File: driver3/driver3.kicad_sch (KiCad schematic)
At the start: 23 parts, among them J1 Conn_02x08_Odd_Even, J2 Conn_02x08_Counter_Clockwise, J3 Conn_01x05, J4 Conn_01x03_Pin, SW1 SW_DIP_x02, SW2 SW_DIP_x02, U1 MP6605CGR-Z

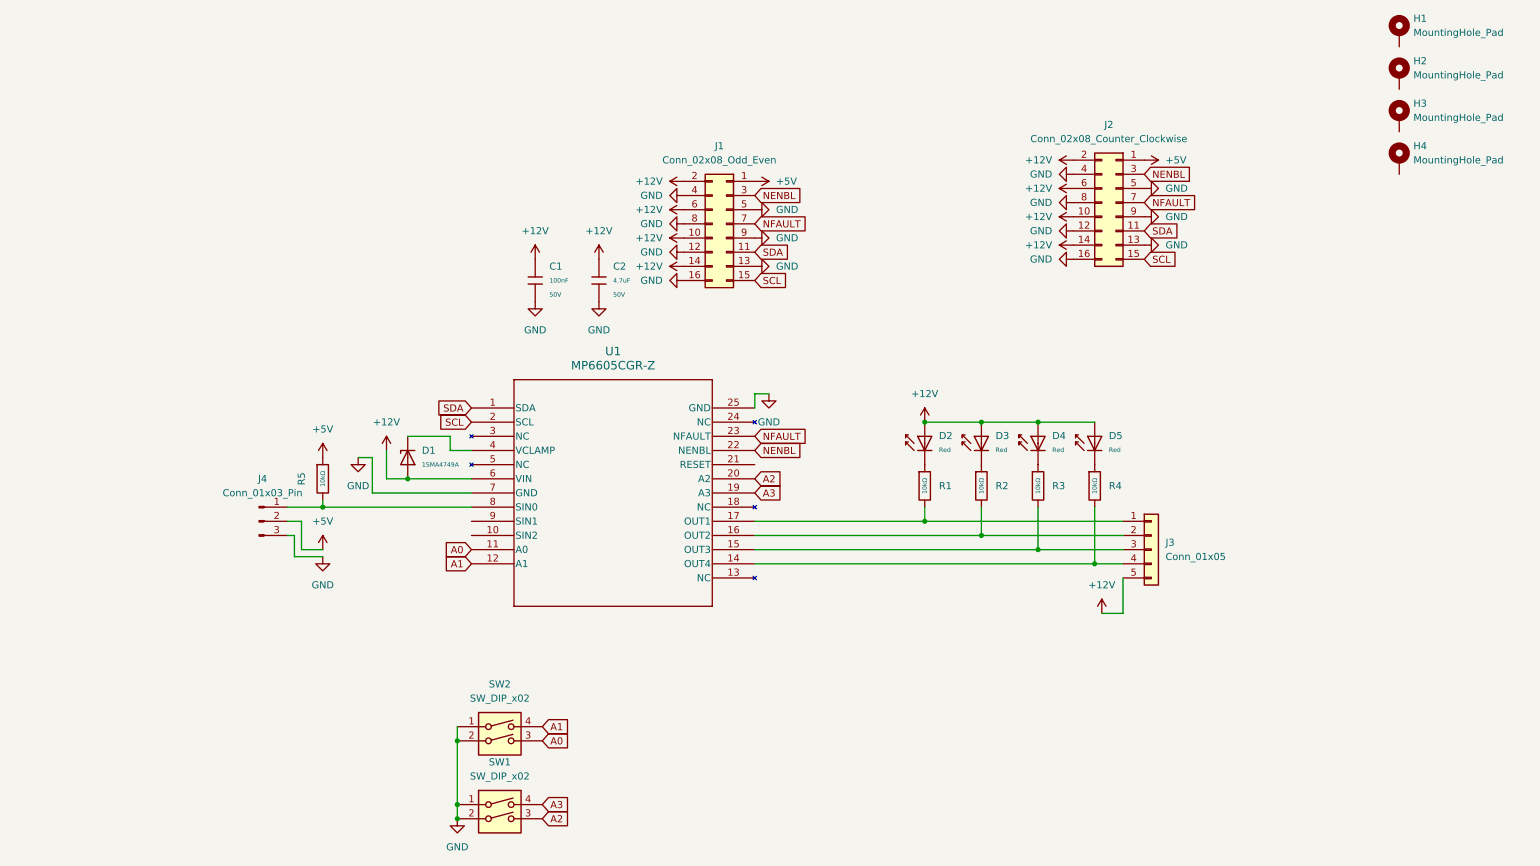
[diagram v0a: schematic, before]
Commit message: Add new driver and web client
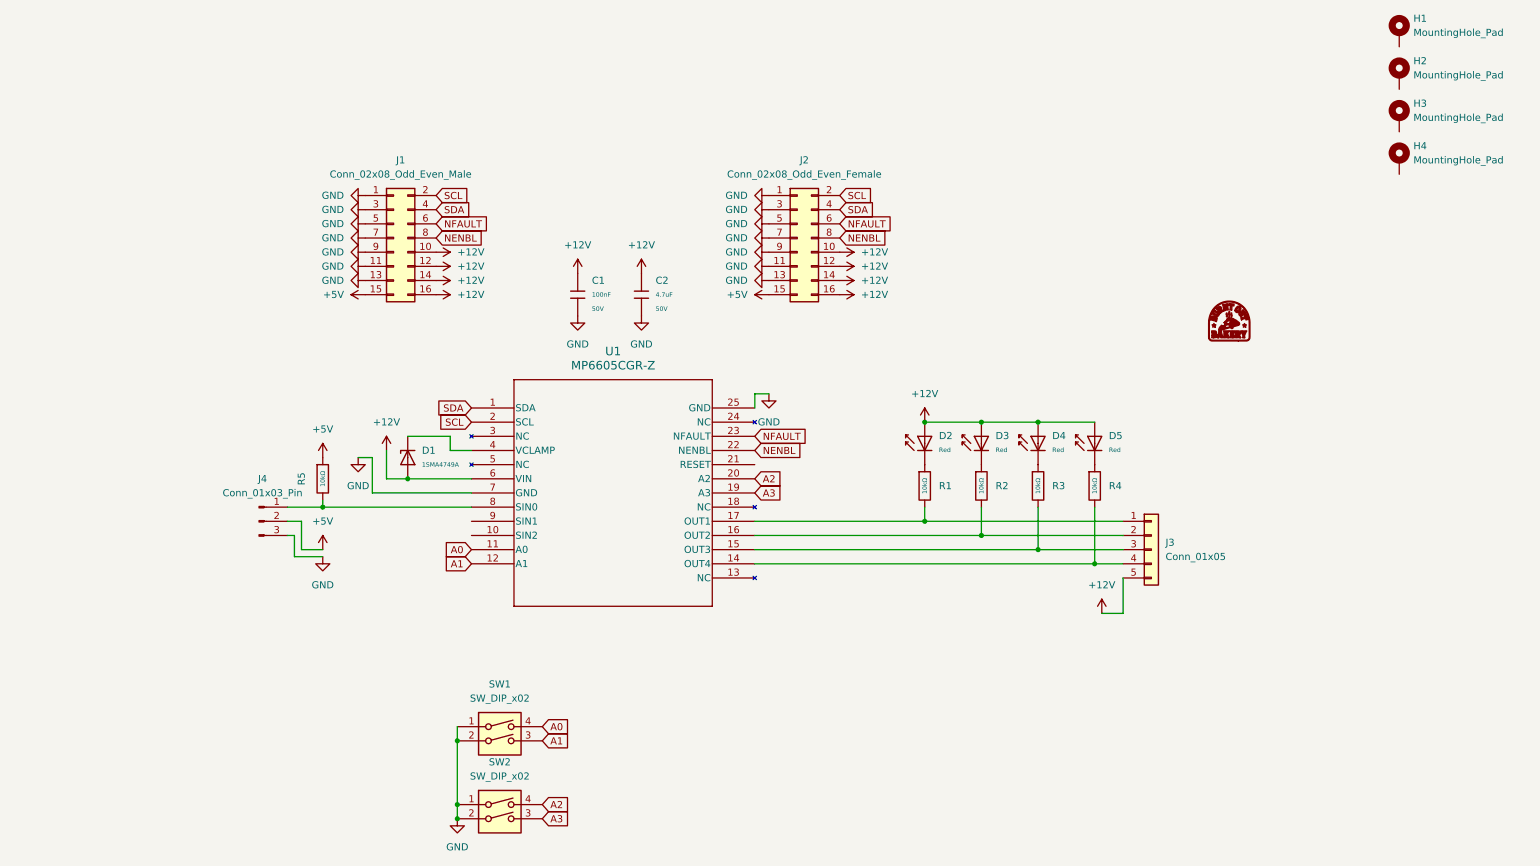
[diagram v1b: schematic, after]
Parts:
- added G1: LOGO, BurntOutBakery:BurntOutBakery, symbol BurntOutBakery:LOGO
- J1: value Conn_02x08_Odd_Even -> Conn_02x08_Odd_Even_Male
- J2: value Conn_02x08_Counter_Clockwise -> Conn_02x08_Odd_Even_Female
- renumbered SW2 to SW1, SW1 to SW2
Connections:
- net +12V: now also J1.12 (Pin_12), J1.16 (Pin_16), J2.12 (Pin_12), J2.16 (Pin_16); no longer J1.2 (Pin_2), J1.6 (Pin_6), J2.2 (Pin_2), J2.6 (Pin_6)
- net +5V: now also J1.15 (Pin_15), J2.15 (Pin_15); no longer J1.1 (Pin_1), J2.1 (Pin_1)
- net A0: now also SW1.4; no longer SW1.3
- net A1: now also SW1.3; no longer SW1.4
- net A2: now also SW2.4; no longer SW2.3
- net A3: now also SW2.3; no longer SW2.4
- net GND: now also J1.1 (Pin_1), J1.11 (Pin_11), J1.3 (Pin_3), J1.7 (Pin_7), J2.1 (Pin_1), J2.11 (Pin_11), J2.3 (Pin_3), J2.7 (Pin_7); no longer J1.12 (Pin_12), J1.16 (Pin_16), J1.4 (Pin_4), J1.8 (Pin_8), J2.12 (Pin_12), J2.16 (Pin_16), J2.4 (Pin_4), J2.8 (Pin_8)
- net NENBL: now also J1.8 (Pin_8), J2.8 (Pin_8); no longer J1.3 (Pin_3), J2.3 (Pin_3)
- net NFAULT: now also J1.6 (Pin_6), J2.6 (Pin_6); no longer J1.7 (Pin_7), J2.7 (Pin_7)
- net SCL: now also J1.2 (Pin_2), J2.2 (Pin_2); no longer J1.15 (Pin_15), J2.15 (Pin_15)
- net SDA: now also J1.4 (Pin_4), J2.4 (Pin_4); no longer J1.11 (Pin_11), J2.11 (Pin_11)
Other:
- moved on the sheet: C1, C2, J1, J2

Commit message: Go back to DRV8804 based design because the MP6605CGR seems to be out of stock.
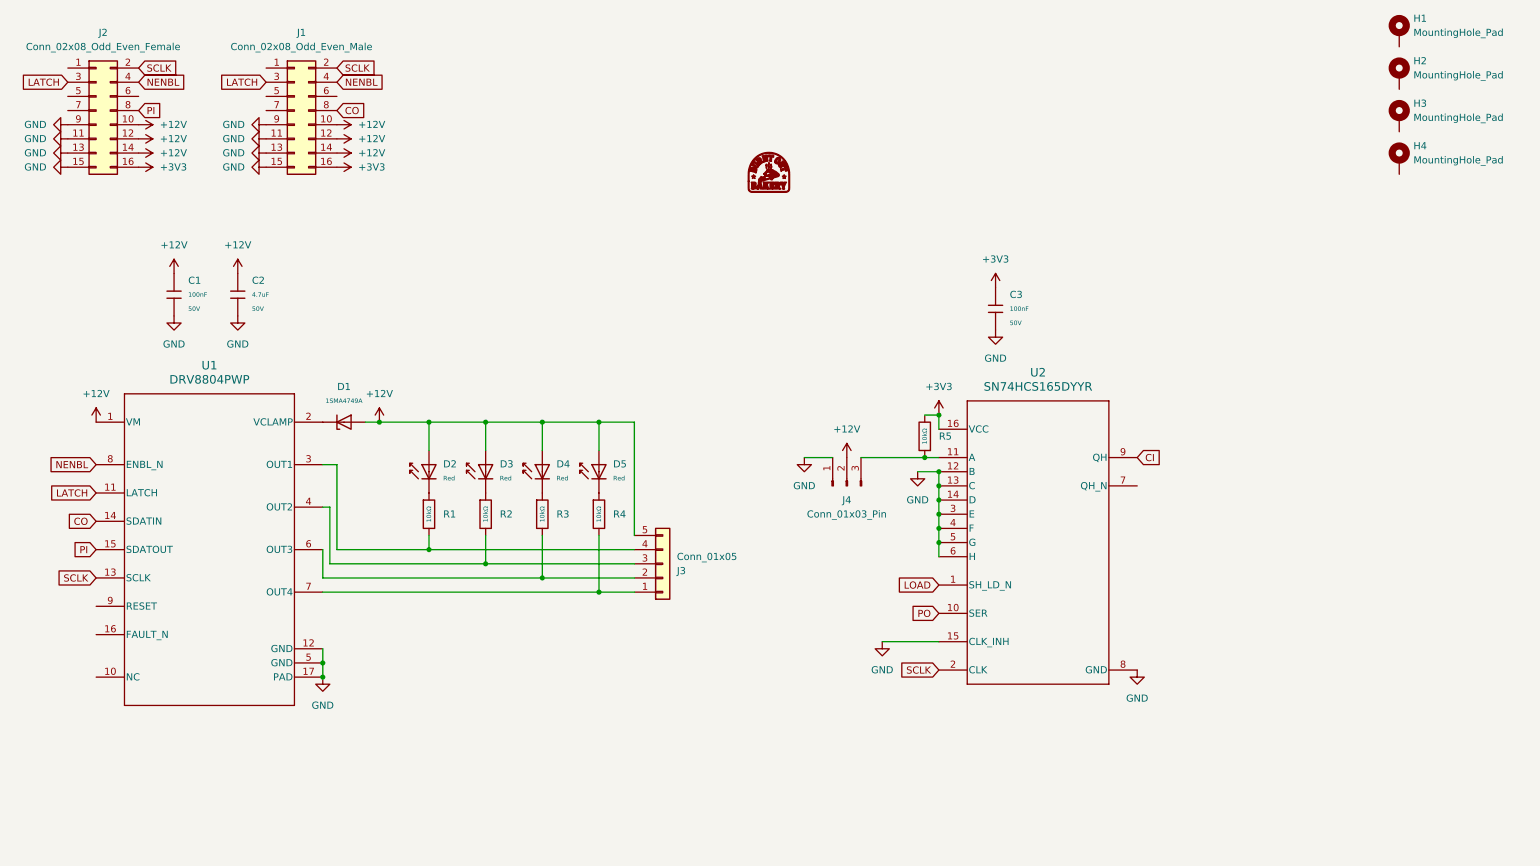
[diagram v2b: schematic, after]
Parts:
- removed SW1, SW2: SW_DIP_x02, Button_Switch_THT:SW_DIP_SPSTx02_Slide_9.78x7.26mm_W7.62mm_P2.54mm, symbol Switch:SW_DIP_x02
- removed U1: MP6605CGR-Z, QFN-24_MP6605C_MNP, symbol ul_MP6605CGR-Z:MP6605CGR-Z
- added C3: 100nF, PCM_JLCPCB:C_0603, symbol PCM_JLCPCB-Capacitors:0603,100nF
- added U1: DRV8804PWP, Package_SO:HTSSOP-16-1EP_4.4x5mm_P0.65mm_EP3.4x5mm_Mask3x3mm_ThermalVias, symbol ul_DRV8804PWP:DRV8804PWP
- added U2: SN74HCS165DYYR, DYY0016A-MFG, symbol ul_SN74HCS165DYYR:SN74HCS165DYYR
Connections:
- net SDA is gone; now on net NENBL: J1.4 (Pin_4), J2.4 (Pin_4)
- net +12V: now also J4.2 (Pin_2), U1.1 (VM); no longer J1.16 (Pin_16), J2.16 (Pin_16)
- net GND: now also J1.15 (Pin_15), J2.15 (Pin_15), J4.1 (Pin_1), C3.2, U1.12 (GND), U1.17 (PAD), U1.5 (GND), U2.12 (B), U2.13 (C), U2.14 (D), U2.15 (CLK_INH), U2.3 (E), U2.4 (F), U2.5 (G), U2.6 (H), U2.8 (GND); no longer J1.1 (Pin_1), J1.3 (Pin_3), J1.5 (Pin_5), J1.7 (Pin_7), J2.1 (Pin_1), J2.3 (Pin_3), J2.5 (Pin_5), J2.7 (Pin_7), J4.3 (Pin_3)
- net NENBL: now also U1.8 (ENBL_N); no longer J1.8 (Pin_8), J2.8 (Pin_8)
- net at R4.2: now also J3.1 (Pin_1), U1.7 (OUT4); no longer J3.4 (Pin_4)
- net at J3.3 (Pin_3): now also R2.2, U1.4 (OUT2); no longer R3.2
- net at J3.2 (Pin_2): now also R3.2, U1.6 (OUT3); no longer R2.2
- net at R1.2: now also J3.4 (Pin_4), U1.3 (OUT1); no longer J3.1 (Pin_1)
- net at D1.1: now also U1.2 (VCLAMP)
- net +3V3: now reaches R5.2
- net +3V3: now also J1.16 (Pin_16), J2.16 (Pin_16), C3.1, U2.16 (VCC); no longer J4.1 (Pin_1)
- removed net +5V: J1.15 (Pin_15), J2.15 (Pin_15), J4.2 (Pin_2), R5.1
- net NFAULT: no longer names the net of J1.6 (Pin_6)
- net NFAULT: no longer J2.6 (Pin_6)
- net SCL renamed SCLK
- net SCLK: now also U1.13 (SCLK), U2.2 (CLK)
- new net: J4.3 (Pin_3), R5.1, U2.11 (A)
- new net CI: U2.9 (QH)
- new net CO: J1.8 (Pin_8), U1.14 (SDATIN)
- new net LATCH: J1.3 (Pin_3), J2.3 (Pin_3), U1.11 (LATCH)
- new net LOAD: U2.1 (SH_LD_N)
- new net PI: J2.8 (Pin_8), U1.15 (SDATOUT)
- new net PO: U2.10 (SER)
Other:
- moved on the sheet: C1, C2, D1, D2, D3, D4, D5, J1, J2, J3, R1, R2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

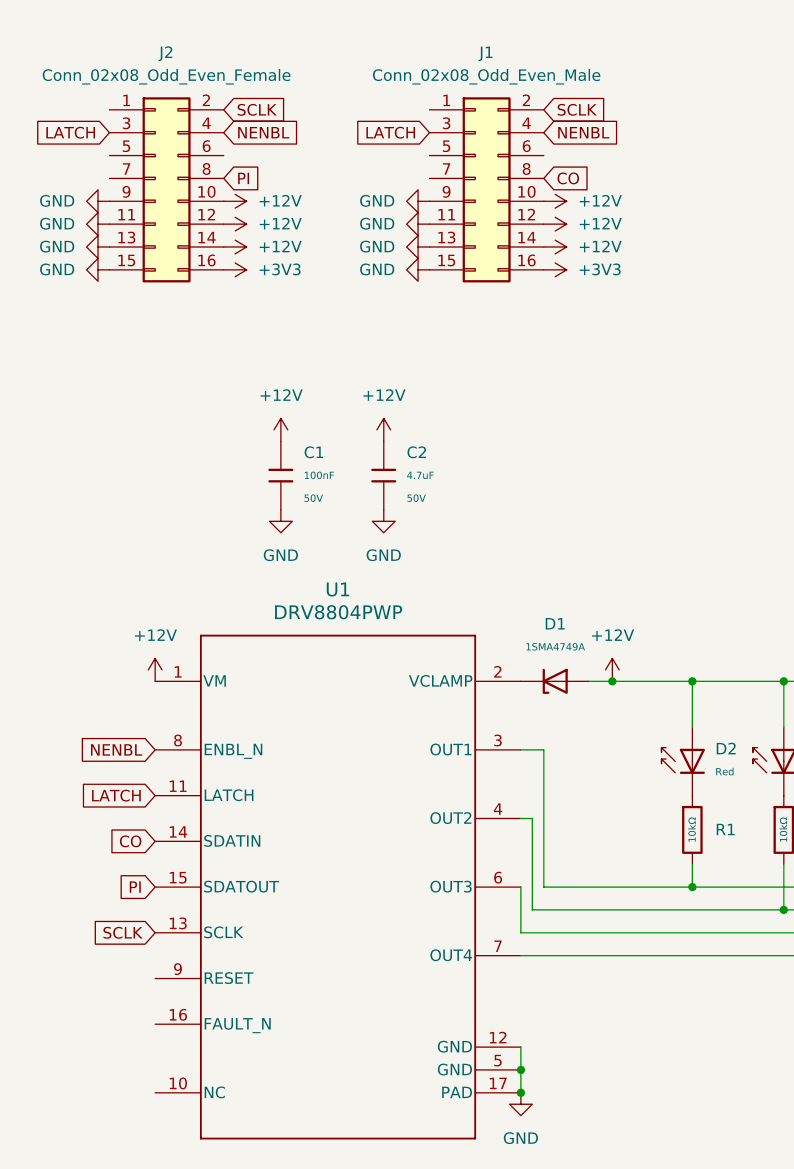
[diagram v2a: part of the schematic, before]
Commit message: Add picotool reset support.
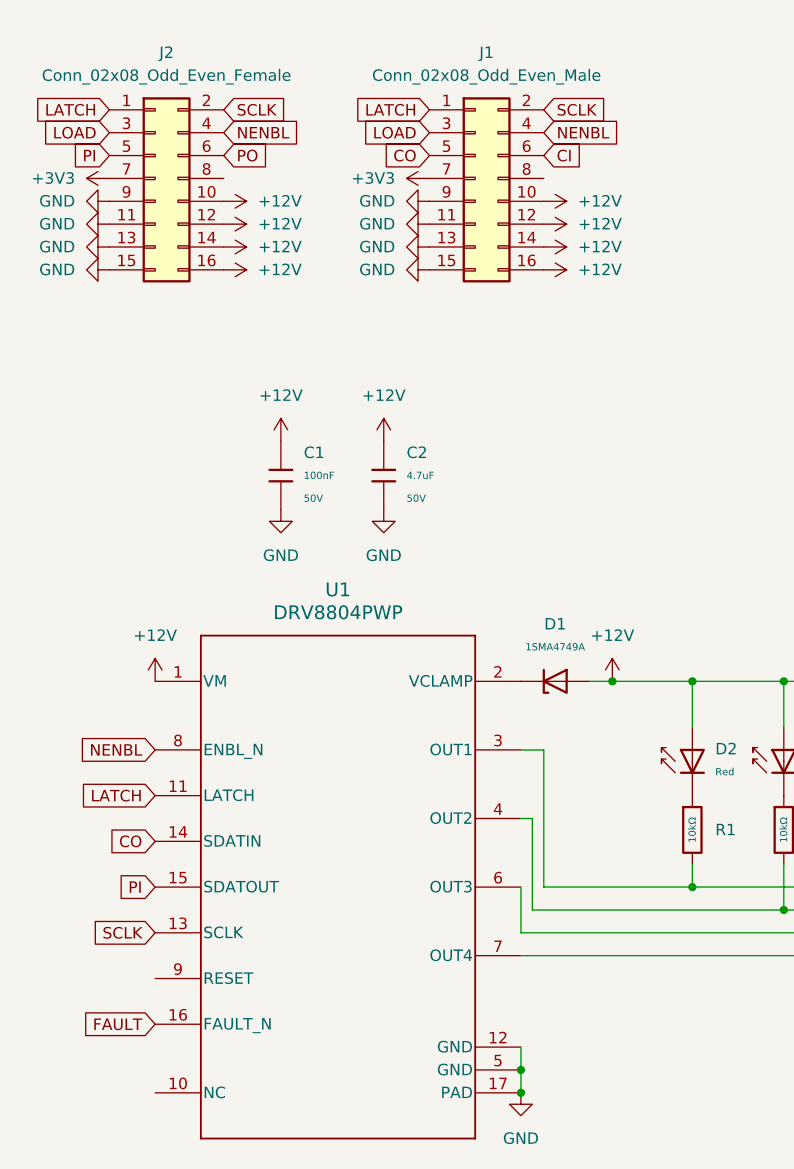
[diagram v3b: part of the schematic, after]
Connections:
- net +12V: now also J1.16 (Pin_16), J2.16 (Pin_16)
- net +3V3: now also J1.7 (Pin_7), J2.7 (Pin_7); no longer J1.16 (Pin_16), J2.16 (Pin_16)
- net CI: now also J1.6 (Pin_6)
- net CO: now also J1.5 (Pin_5); no longer J1.8 (Pin_8)
- net LATCH: now also J1.1 (Pin_1), J2.1 (Pin_1); no longer J1.3 (Pin_3), J2.3 (Pin_3)
- net LOAD: now also J1.3 (Pin_3), J2.3 (Pin_3)
- net PI: now also J2.5 (Pin_5); no longer J2.8 (Pin_8)
- net PO: now also J2.6 (Pin_6)
- net FAULT: now reaches U1.16 (FAULT_N)
